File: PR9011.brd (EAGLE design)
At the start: 148 x 100 mm, 69 parts, among them J1 M3_SCREW_POST, SW1 SPST_TACT-KMR2, Y1 32.768kHz

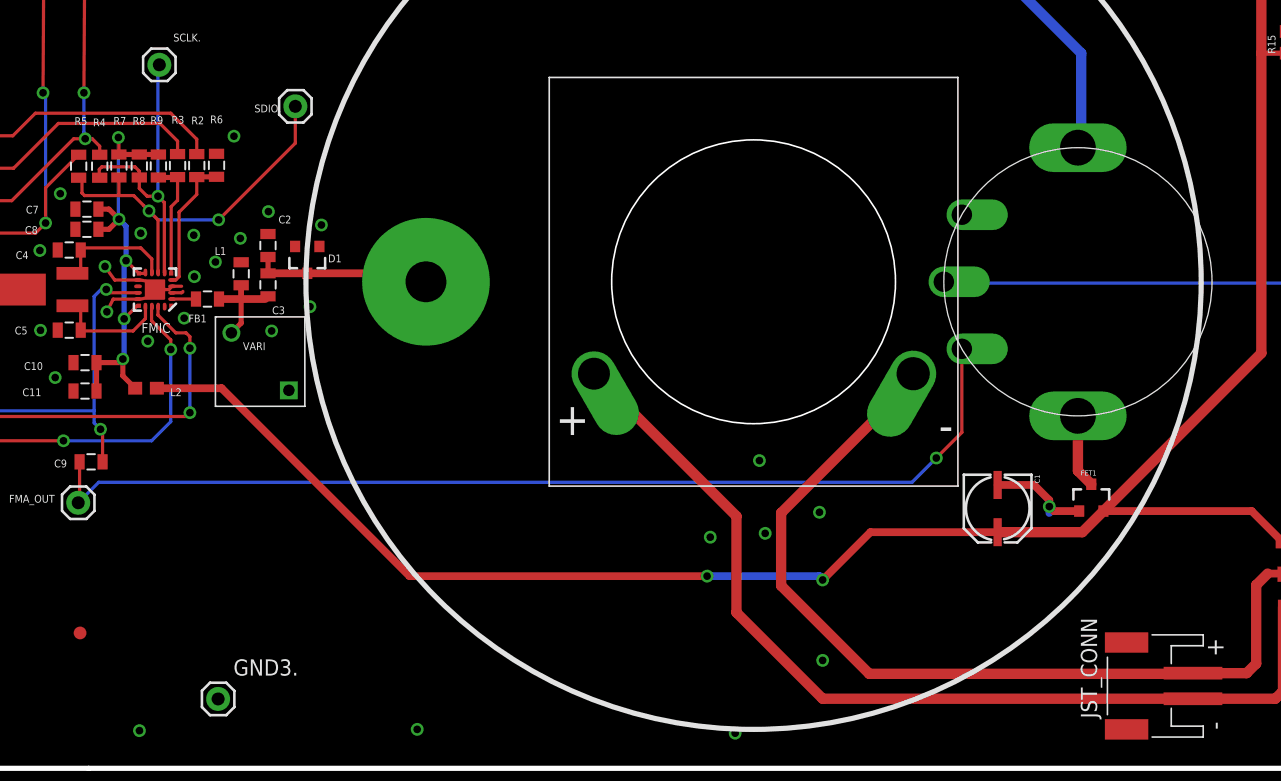
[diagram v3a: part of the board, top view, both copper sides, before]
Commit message: changed speaker to JST
added screw holes, removed pads on speaker. re-routed a couple of
traces.
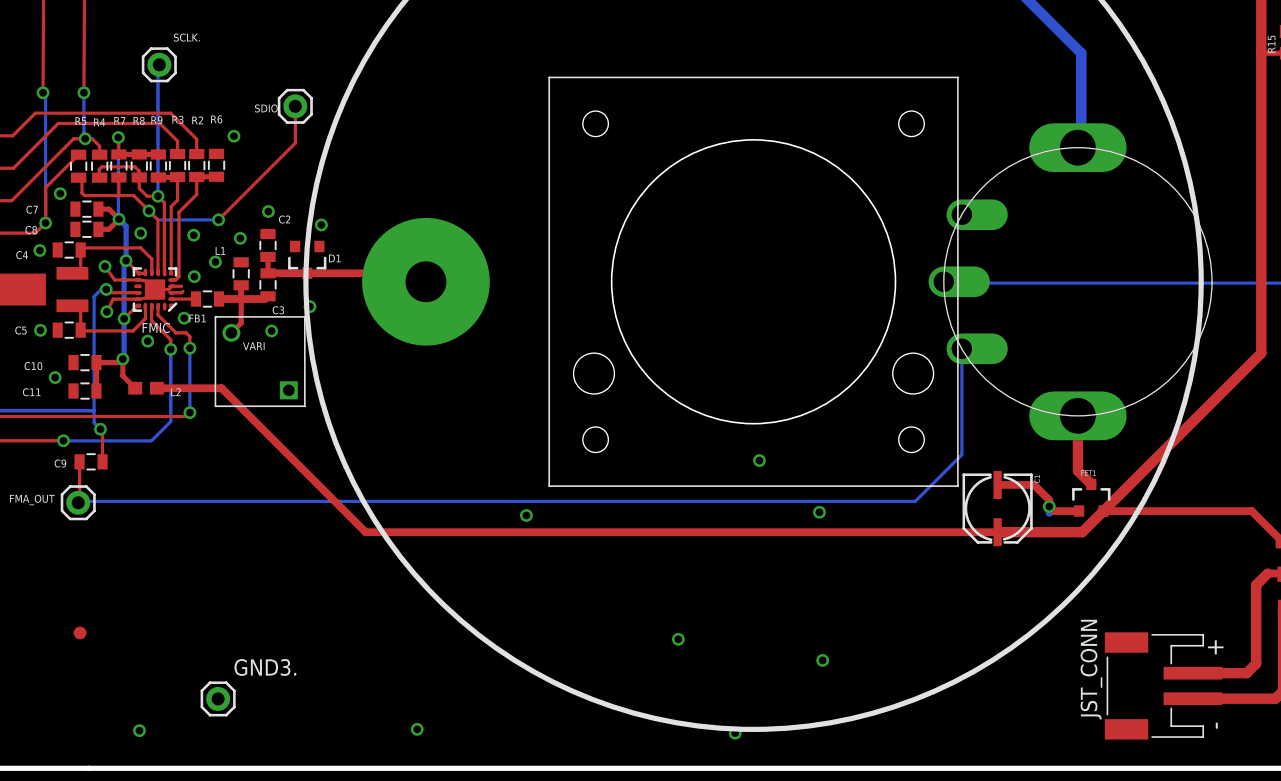
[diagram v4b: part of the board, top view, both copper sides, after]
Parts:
- removed U$3: CE32A_DAYTON_SPKR, PR_Libraries:CE32A_DAYTON_SPKR
- added U$5: CE32A_FOR_JST, PR_Libraries:CE32A_FOR_JST
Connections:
- net N$9: no longer U$3.-
- net OUT-: no longer U$3.+
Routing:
- net OUT-: track 75.7 -> 13.8 mm
- net N$9: track 70.4 -> 13.9 mm
- net VCC: track 185.8 -> 182.7 mm, vias 3 -> 1
- net A_IN: track 81.3 -> 82.3 mm, vias 1 -> 0
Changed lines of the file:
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@@
 <?xml version="1.0" encoding="utf-8"?>
 <!DOCTYPE eagle SYSTEM "eagle.dtd">
-<eagle version="6.6.0">
+<eagle version="7.2.0">
 <drawing>
 <settings>
@@
 <pass name="Default">
 <param name="RoutingGrid" value="50mil"/>
+<param name="AutoGrid" value="1"/>
+<param name="Efforts" value="0"/>
+<param name="TopRouterVariant" value="1"/>
 <param name="tpViaShape" value="round"/>
 <param name="PrefDir.1" value="|"/>
@@
 <element name="JP5" library="PR_Libraries" package="BK-92_MPD_AA_BATT_CLIP" value="BK-92_MPD_AA_BATT_CLIP" x="114.742" y="89.662"/>
 <element name="JP6" library="PR_Libraries" package="BK-92_MPD_AA_BATT_CLIP" value="BK-92_MPD_AA_BATT_CLIP" x="54.29" y="89.662"/>
-<element name="U$3" library="PR_Libraries" package="CE32A_DAYTON_SPKR" value="CE32A_DAYTON_SPKR" x="73.34" y="38.1"/>
 <element name="FB1" library="SparkFun-Passives" package="0805" value="" x="30.578" y="36.75" smashed="yes" rot="R180">
 <attribute name="NAME" x="30.513" y="35.53" size="0.6096" layer="25" rot="R180"/>
@@
 <element name="U$2" library="adafruit" package="FIDUCIAL_1MM" value="FIDUCIAL" x="6.1" y="90.7"/>
 <element name="U$4" library="adafruit" package="FIDUCIAL_1MM" value="FIDUCIAL" x="20.6" y="10.6"/>
+<element name="U$5" library="PR_Libraries" package="CE32A_FOR_JST" value="CE32A_FOR_JST" x="73.34" y="38.1" locked="yes"/>
 </elements>
 <signals>
@@
 <via x="78.5" y="20.05" extent="1-16" drill="0.6"/>
 <via x="78.75" y="8.45" extent="1-16" drill="0.6"/>
-<via x="69.95" y="18.1" extent="1-16" drill="0.6"/>
+<via x="55.55" y="19.8" extent="1-16" drill="0.6"/>
 <via x="71.9" y="2.75" extent="1-16" drill="0.6"/>
-<via x="74.25" y="18.4" extent="1-16" drill="0.6"/>
+<via x="67.45" y="10.1" extent="1-16" drill="0.6"/>
 <via x="2.9" y="2.95" extent="1-16" drill="0.6"/>
 <via x="25.25" y="2.95" extent="1-16" drill="0.6"/>
@@
 <wire x1="112.348" y1="20.144" x2="100.736" y2="20.144" width="0.6096" layer="1"/>
 <wire x1="26.616" y1="29.764" x2="31.686" y2="29.764" width="0.6096" layer="1"/>
-<wire x1="31.686" y1="29.764" x2="46.4" y2="15.05" width="0.6096" layer="1"/>
-<wire x1="46.4" y1="15.05" x2="69.7" y2="15.05" width="0.6096" layer="1"/>
-<via x="69.7" y="15.05" extent="1-16" drill="0.6"/>
-<wire x1="69.7" y1="15.05" x2="78.45" y2="15.05" width="0.6096" layer="16"/>
-<wire x1="78.45" y1="15.05" x2="78.75" y2="14.75" width="0.6096" layer="16" curve="-90"/>
-<via x="78.75" y="14.75" extent="1-16" drill="0.6"/>
-<wire x1="78.75" y1="14.75" x2="82.49" y2="18.49" width="0.6096" layer="1"/>
-<wire x1="82.49" y1="18.49" x2="92.452" y2="18.49" width="0.6096" layer="1"/>
 <contactref element="R15" pad="1"/>
 <wire x1="115.1" y1="56" x2="113.102" y2="56" width="0.4064" layer="1"/>
+<wire x1="31.686" y1="29.764" x2="42.96" y2="18.49" width="0.6096" layer="1"/>
+<wire x1="42.96" y1="18.49" x2="92.452" y2="18.49" width="0.6096" layer="1"/>
 </signal>
 <signal name="N$4">
@@
 </signal>
 <signal name="OUT-">
-<contactref element="U$3" pad="+"/>
 <contactref element="FB3" pad="1"/>
 <wire x1="114.8" y1="12.6" x2="114.8" y2="6.05" width="0.8128" layer="1"/>
@@
 <wire x1="114.8" y1="6.05" x2="114.2" y2="5.45" width="0.8128" layer="1"/>
 <wire x1="114.2" y1="5.45" x2="107.75" y2="5.45" width="0.8128" layer="1"/>
-<wire x1="107.75" y1="5.45" x2="78.75" y2="5.45" width="0.8128" layer="1"/>
-<wire x1="78.75" y1="5.45" x2="72" y2="12.2" width="0.8128" layer="1"/>
-<wire x1="72" y1="12.2" x2="72" y2="19.74" width="0.8128" layer="1"/>
-<wire x1="72" y1="19.74" x2="60.84" y2="30.9" width="0.8128" layer="1"/>
 </signal>
 <signal name="N$34">
@@
 <contactref element="C9" pad="2"/>
 <contactref element="FMA_OUT" pad="1"/>
-<wire x1="89.65" y1="32.85" x2="89.65" y2="26.3" width="0.254" layer="1"/>
-<wire x1="89.65" y1="26.3" x2="87.65" y2="24.3" width="0.254" layer="1"/>
-<via x="87.65" y="24.3" extent="1-16" drill="0.6"/>
-<wire x1="87.65" y1="24.3" x2="85.75" y2="22.4" width="0.254" layer="16"/>
-<wire x1="85.75" y1="22.4" x2="22.06" y2="22.4" width="0.254" layer="16"/>
-<wire x1="22.06" y1="22.4" x2="20.456" y2="20.796" width="0.254" layer="16"/>
 <wire x1="20.562" y1="24" x2="20.562" y2="20.902" width="0.254" layer="1"/>
 <wire x1="20.562" y1="20.902" x2="20.456" y2="20.796" width="0.254" layer="1"/>
+<wire x1="89.65" y1="32.85" x2="89.65" y2="24.55" width="0.254" layer="16"/>
+<wire x1="89.65" y1="24.55" x2="86" y2="20.9" width="0.254" layer="16"/>
+<wire x1="86" y1="20.9" x2="20.56" y2="20.9" width="0.254" layer="16"/>
+<wire x1="20.56" y1="20.9" x2="20.456" y2="20.796" width="0.254" layer="16"/>
 </signal>
 <signal name="N$3">
@@
 </signal>
 <signal name="N$9">
-<contactref element="U$3" pad="-"/>
 <contactref element="FB2" pad="2"/>
 <contactref element="JST_CONN" pad="1"/>
@@
 <wire x1="113.6" y1="15.25" x2="114.714" y2="15.25" width="0.6096" layer="1"/>
 <wire x1="114.714" y1="15.25" x2="114.764" y2="15.2" width="0.6096" layer="1"/>
-<wire x1="85.84" y1="30.9" x2="85.84" y2="30.34" width="0.8128" layer="1"/>
-<wire x1="85.84" y1="30.34" x2="75.5" y2="20" width="0.8128" layer="1"/>
-<wire x1="75.5" y1="20" x2="75.5" y2="14.3" width="0.8128" layer="1"/>
-<wire x1="75.5" y1="14.3" x2="82.4" y2="7.4" width="0.8128" layer="1"/>
-<wire x1="82.4" y1="7.4" x2="108.25" y2="7.4" width="0.8128" layer="1"/>
 <wire x1="108.25" y1="7.4" x2="108.3" y2="7.45" width="0.6096" layer="1"/>
 </signal>
